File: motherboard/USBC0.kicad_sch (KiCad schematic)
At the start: 26 parts, among them J5 Outer USB-C, J9 Inner USB-C, U1 TPD4E02B04, U15 TVS2200DRV, U2 TPD4E02B04, U3 TPD4E02B04, U4 FUSB302BMPX, U5 SY6280AAC

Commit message: v0.2 layout
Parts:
- removed J9: Inner USB-C, USB-C:USB-C-SMD_TYPE-C-24P-QT, symbol Connector:USB_C_Receptacle
- removed R122: 1M, Resistor_SMD:R_0402_1005Metric, symbol Device:R_Small

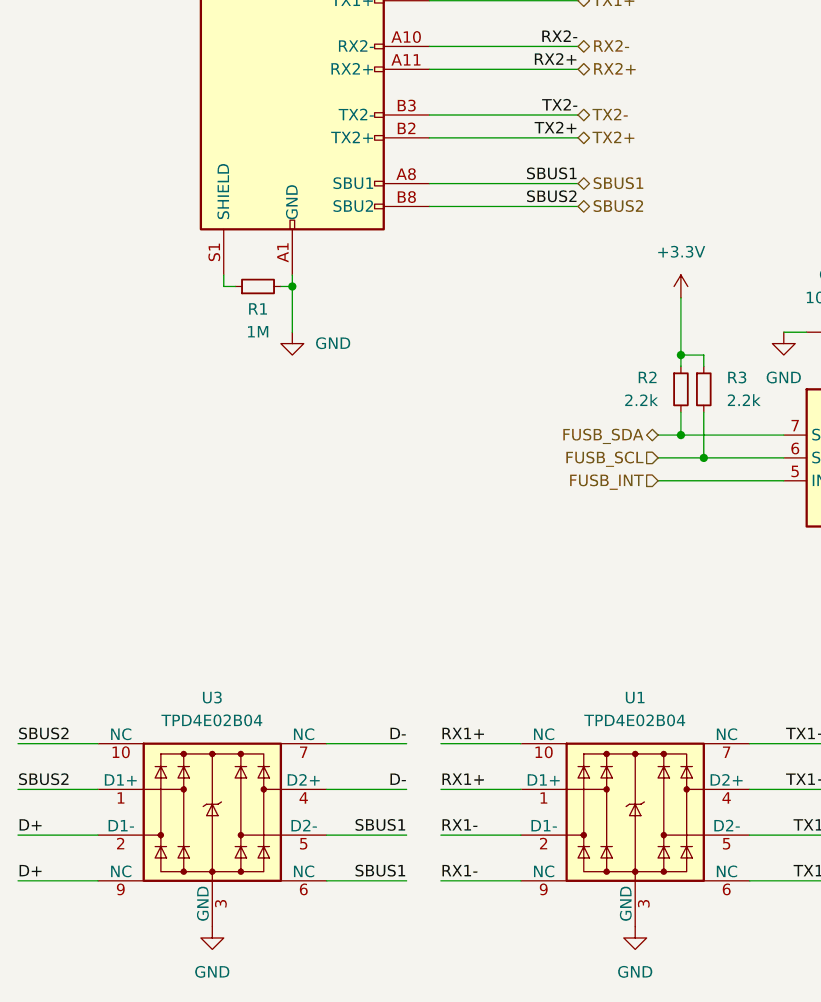
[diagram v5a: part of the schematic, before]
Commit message: v0.2 < 50 unrouted
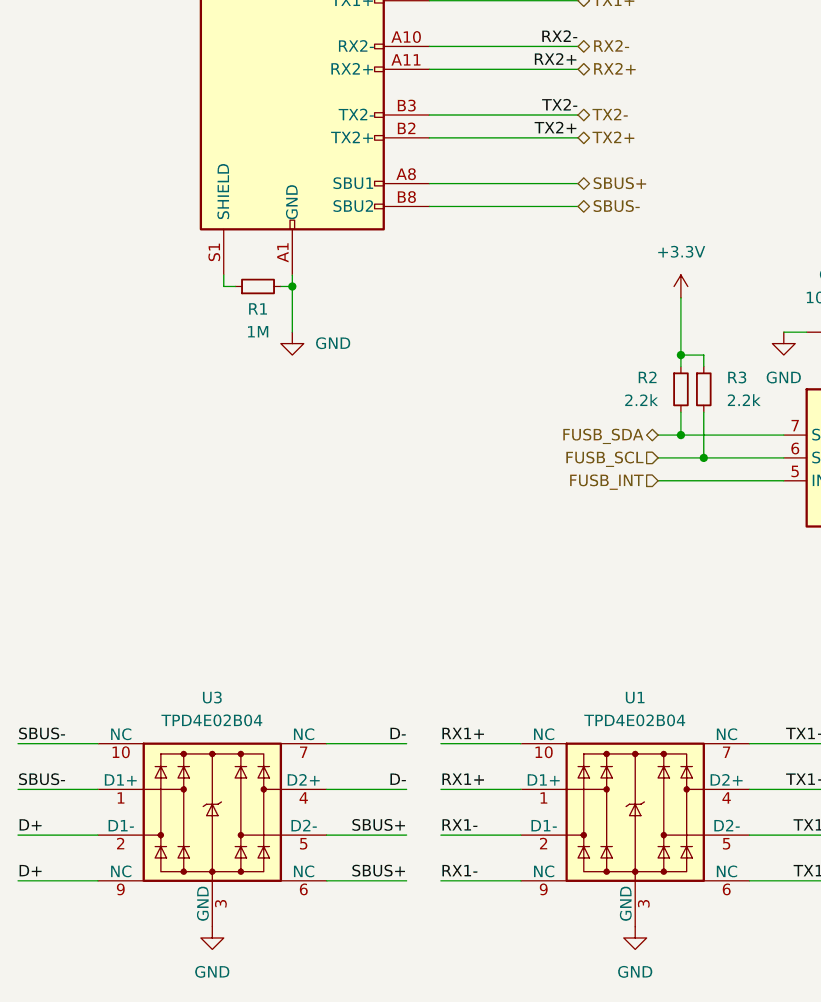
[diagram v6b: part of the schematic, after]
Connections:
- net SBUS1 renamed SBUS+
- net SBUS2 renamed SBUS-
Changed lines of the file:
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@@
-		)
-	)
-	(label "SBUS1"
-		(at 77.47 106.68 180)
-		(fields_autoplaced yes)
-		(effects
-			(font
-				(size 1.27 1.27)
-			)
-			(justify right bottom)
 		)
 	)
@@
 		)
 	)
-	(label "SBUS2"
-		(at 77.47 109.22 180)
-		(fields_autoplaced yes)
-		(effects
-			(font
-				(size 1.27 1.27)
-			)
-			(justify right bottom)
-		)
-	)
 	(label "TX1-"
 		(at 105.41 184.15 180)
@@
 		)
 	)
-	(label "SBUS2"
+	(label "SBUS-"
 		(at 15.24 168.91 0)
 		(fields_autoplaced yes)
@@
 		)
 	)
-	(label "SBUS2"
+	(label "SBUS-"
 		(at 15.24 173.99 0)
 		(fields_autoplaced yes)
@@
 		)
 	)
-	(label "SBUS1"
+	(label "SBUS+"
 		(at 58.42 184.15 180)
 		(fields_autoplaced yes)
@@
 		)
 	)
-	(label "SBUS1"
+	(label "SBUS+"
 		(at 58.42 179.07 180)
 		(fields_autoplaced yes)
@@
 		)
 	)
-	(hierarchical_label "SBUS2"
+	(hierarchical_label "SBUS-"
 		(shape bidirectional)
 		(at 77.47 109.22 0)
@@
 		)
 	)
-	(hierarchical_label "SBUS1"
+	(hierarchical_label "SBUS+"
 		(shape bidirectional)
 		(at 77.47 106.68 0)
